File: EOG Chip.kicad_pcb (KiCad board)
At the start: 2 copper layers, 15 parts, among them U1 INA128, U2 INA128, U3 TL074

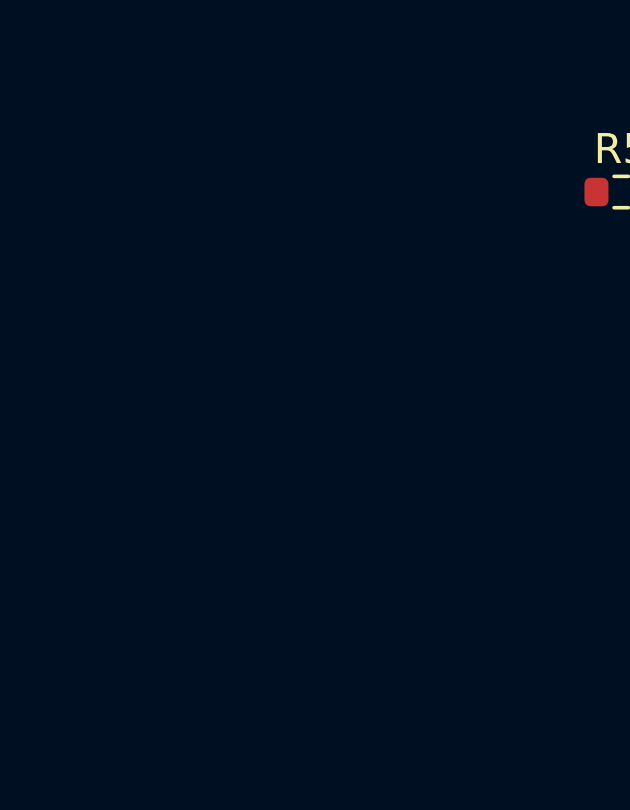
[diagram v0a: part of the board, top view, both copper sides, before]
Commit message: Added footprints for antenna filter module and microcontroller
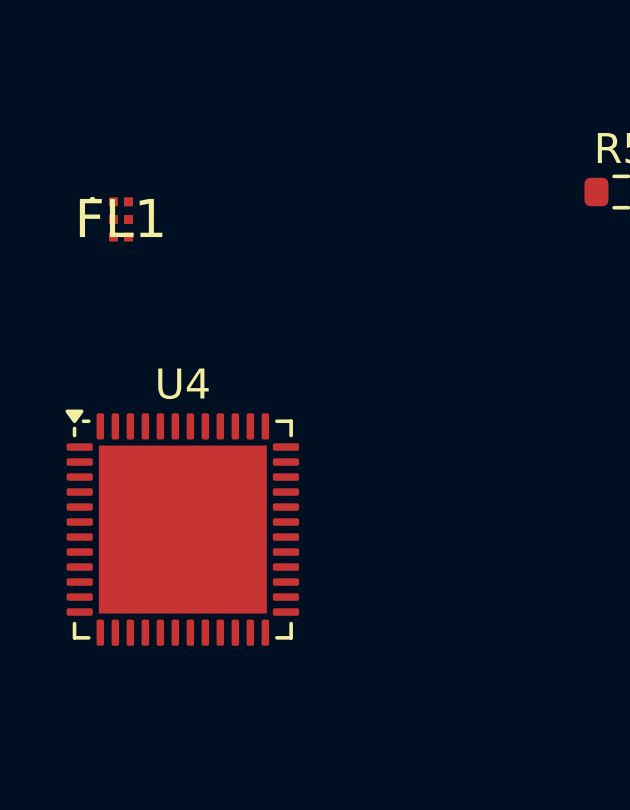
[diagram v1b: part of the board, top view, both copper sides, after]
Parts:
- added FL1: MLPF-WB55-01E3, AntennaFilter_MLPF:BUMPLESS_CSP_2025, F.Cu at (126.5, 86.4)
- added U4: STM32WB55CCUx, Package_DFN_QFN:QFN-48-1EP_7x7mm_P0.5mm_EP5.6x5.6mm, F.Cu at (128.6, 96.8)
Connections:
- R5 pad 2: GND -> GROUND
- R6 pad 1: +5V -> +3V

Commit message: updated files
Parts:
- added AE1: Antenna, antenna_ghz:ANTC3216X60N, F.Cu at (132.5, 107.5)
- added Y1: Crystal, new_crystal:ABM11A32000MHZD2YT3, F.Cu at (179.3, 105.0)
- FL1: footprint AntennaFilter_MLPF:BUMPLESS_CSP_2025 -> a_rf_module:BUMPLESS_CSP_2025
- moved R_GAIN_HOR1 49.2 mm to (114.1, 77.5), turned to 90 degrees
- moved R1 45.2 mm to (152.8, 55.0)
- moved R_GAIN_VERT1 44.0 mm to (114.7, 95.4), turned to 90 degrees
- moved R3 41.4 mm to (129.8, 72.5)
- moved U2 38.3 mm to (121.4, 103.0), turned to 90 degrees
- moved U1 38.1 mm to (121.5, 82.5), turned to 90 degrees
- moved U4 37.6 mm to (165.7, 102.9)
- moved C1 35.9 mm to (139.1, 72.5), turned to 0 degrees
- moved R2 24.8 mm to (170.0, 90.0)
- moved R4 24.7 mm to (128.9, 90.4)
- moved FL1 23.3 mm to (139.8, 105.6)
- moved R5 22.9 mm to (160.0, 70.0)
- moved R6 22.9 mm to (164.5, 70.0)
- moved U3 12.4 mm to (151.2, 77.4)
- moved C2 11.0 mm to (138.9, 90.4), turned to 0 degrees
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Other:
- board outline added: 80 x 50 mm

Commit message: updating schematics
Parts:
- U1, U2: footprint Package_DIP:DIP-8_W7.62mm -> amp_new:SOP65P490X110-8N
- U3: footprint Package_DIP:DIP-14_W7.62mm -> amp_new_big:SOIC127P600X175-14N
- moved C3 34.5 mm to (163.2, 71.0)
- moved R5 24.4 mm to (169.5, 92.5)
- moved R6 24.0 mm to (165.0, 94.0)
- moved R2 23.5 mm to (147.0, 95.0)
- moved R1 16.2 mm to (150.2, 71.0)
- moved FL1 12.5 mm to (152.2, 106.5)
- moved AE1 10.5 mm to (143.0, 107.0)
- moved C4 7.26 mm to (147.0, 101.0)
- moved Y1 6.82 mm to (172.5, 105.0)
- moved C2 4.88 mm to (138.9, 85.5)
- moved R3 4.14 mm to (125.9, 71.0)
- moved R4 2.09 mm to (126.8, 90.4)
- moved C1 1.50 mm to (139.1, 71.0)
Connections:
- U3 pad 13: Net-(U2-Ref) -> Net-(U1-Ref)
- U3 pad 14: Net-(U2-Ref) -> Net-(U1-Ref)
- U3 pad 8: Net-(U1-Ref) -> Net-(U2-Ref)
- U3 pad 9: Net-(U1-Ref) -> Net-(U2-Ref)
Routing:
- added copper zone on B.Cu, net GND
- added copper zone on F.Cu, net GND

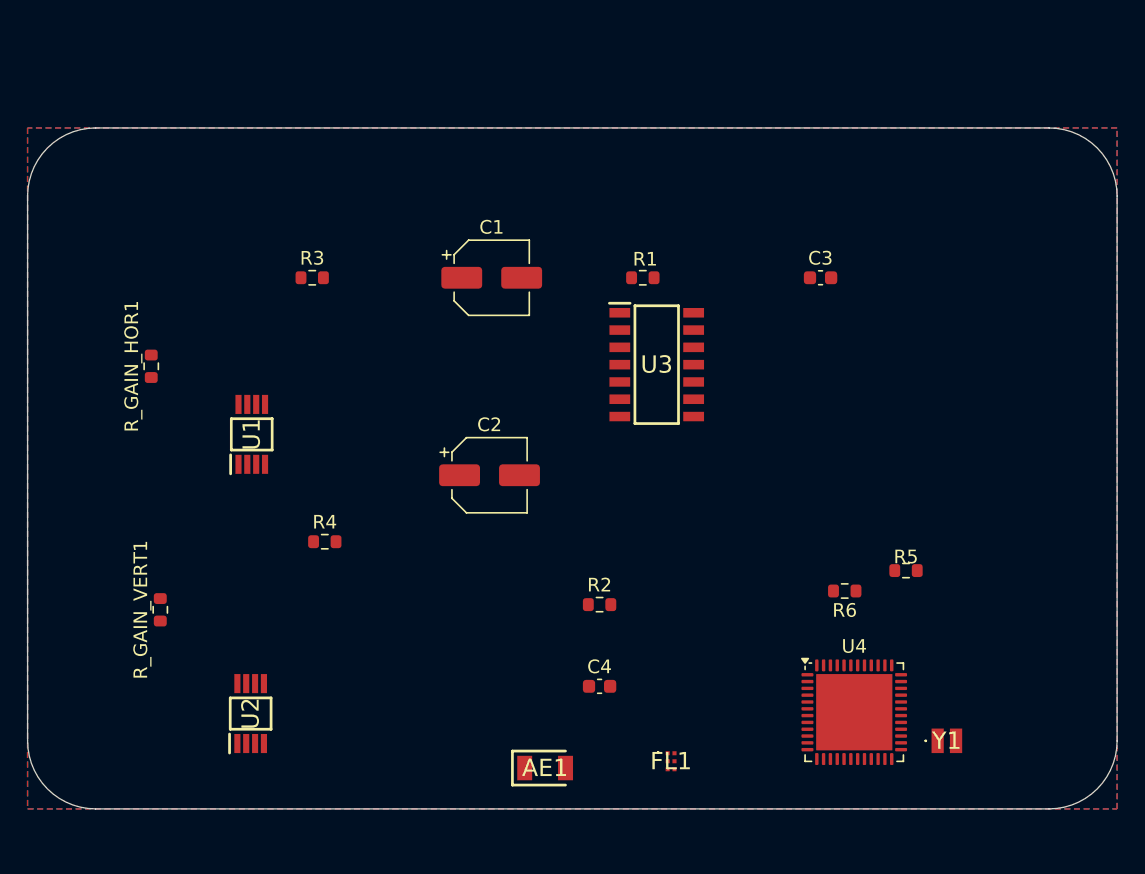
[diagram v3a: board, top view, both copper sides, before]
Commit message: Added potentiometers and started on traces
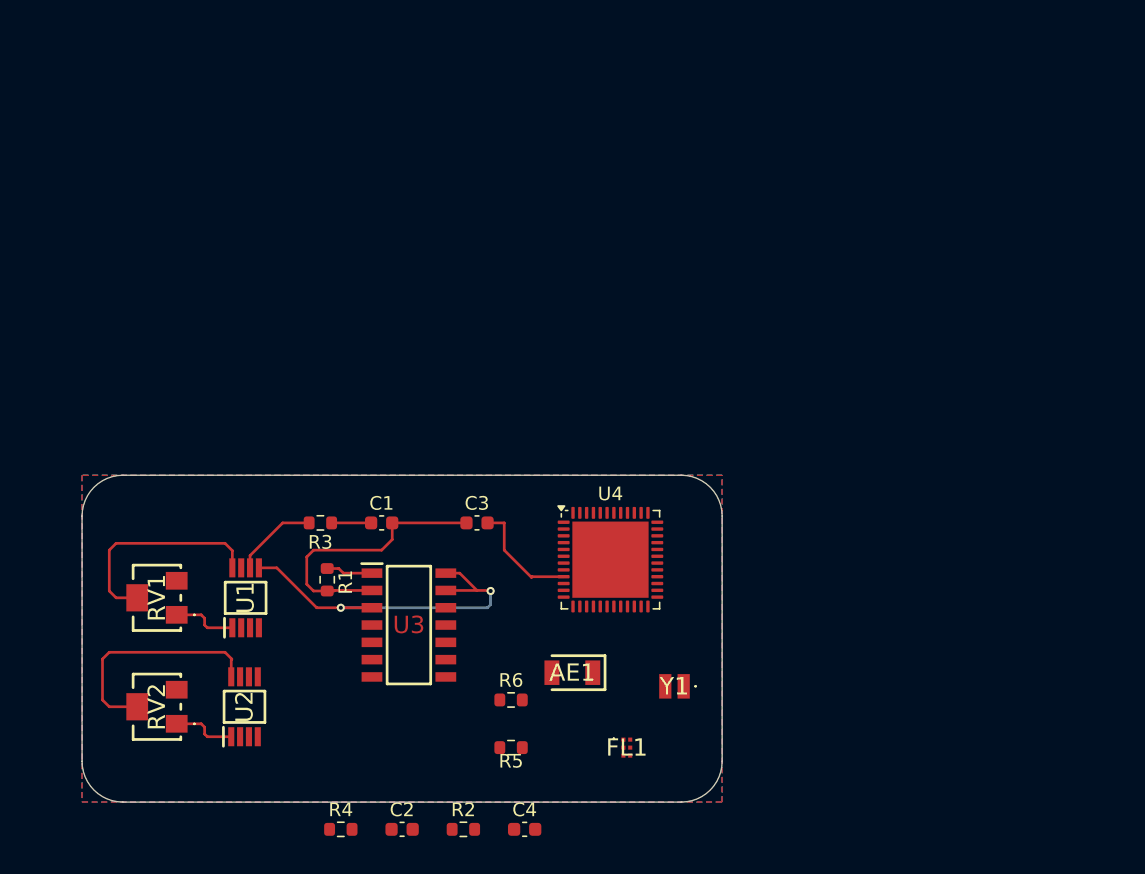
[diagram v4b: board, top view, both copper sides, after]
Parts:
- C1, C2: value C_Polarized_US -> C; footprint Capacitor_SMD:CP_Elec_5x4.5 -> Capacitor_SMD:C_0603_1608Metric
- RV1: renamed from R_GAIN_HOR1; value R -> R_Potentiometer_Hor; footprint Resistor_SMD:R_0603_1608Metric -> Potentiometer_TSM:TSM41YJ503KR05
- RV2: renamed from R_GAIN_VERT1; value R -> R_Potentiometer_Vert; footprint Resistor_SMD:R_0603_1608Metric -> Potentiometer_TSM:TSM41YJ503KR05
- moved R1 32.1 mm to (127.0, 93.2), turned to -90 degrees
- moved R5 31.8 mm to (140.5, 105.5), turned to 180 degrees
- moved C3 31.0 mm to (138.0, 89.0)
- moved C2 26.8 mm to (132.5, 111.5)
- moved U3 26.4 mm to (133.0, 96.5)
- moved R6 25.8 mm to (140.5, 102.0), turned to 0 degrees
- moved R4 21.2 mm to (128.0, 111.5)
- moved U4 21.1 mm to (147.8, 91.7)
- moved Y1 20.4 mm to (152.5, 101.0), turned to 180 degrees
- moved C1 19.7 mm to (131.0, 89.0)
- moved R2 19.3 mm to (137.0, 111.5)
- moved R3 18.0 mm to (126.5, 89.0), turned to 180 degrees
- moved RV1 17.0 mm to (114.5, 94.5)
- moved U1 12.0 mm to (121.0, 94.5)
- moved C4 11.9 mm to (141.5, 111.5)
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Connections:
- U4 pad 10: HOR_OUT -> VERT_OUT
- U4 pad 9: VERT_OUT -> HOR_OUT
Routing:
- net Net-(U1-Ref): track 0.00 -> 27.7 mm, vias 0 -> 2
- net Net-(U3A--): track 0.00 -> 20.5 mm
- net Net-(RV2-Pad2): track 0.00 -> 17.0 mm
- net Net-(RV1-Pad2): track 0.00 -> 16.0 mm
- net HOR_OUT: track 0.00 -> 8.44 mm
- net Net-(R3-Pad2): track 0.00 -> 6.23 mm
- net Net-(RV1-Pad1): track 0.00 -> 4.77 mm
- net Net-(RV2-Pad1): track 0.00 -> 4.69 mm
- net Net-(R1-Pad1): track 0.00 -> 3.45 mm
- net Net-(C1-Pad1): track 0.00 -> 2.90 mm
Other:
- board size 80 x 50 mm -> 47 x 24 mm

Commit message: Add files via upload
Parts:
- moved R2 14.1 mm to (126.8, 101.8), turned to -90 degrees
- moved C4 8.68 mm to (135.3, 105.4)
- moved R4 6.98 mm to (125.0, 105.2), turned to 180 degrees
- moved C2 6.84 mm to (129.6, 105.3)
- moved AE1 1.65 mm to (145.4, 101.6)
- moved Y1 0.29 mm to (152.8, 100.9)
- turned R5 to 0 degrees
- turned R6 to 180 degrees
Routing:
- net Net-(U2-Ref): track 0.00 -> 23.9 mm, vias 0 -> 3
- net Net-(FL1-IN): track 0.00 -> 17.7 mm
- net VERT_OUT: track 0.00 -> 16.5 mm
- net REF_IN: track 0.00 -> 15.8 mm, vias 0 -> 2
- net +3V: track 0.00 -> 13.0 mm
- net Net-(R4-Pad2): track 0.00 -> 10.8 mm
- net Net-(U3B--): track 0.00 -> 10.2 mm
- net Net-(U4-OSC_IN): track 0.00 -> 8.25 mm
- net Net-(U4-OSC_OUT): track 0.00 -> 6.40 mm
- net Net-(AE1-A): track 0.00 -> 4.90 mm
- net Net-(R2-Pad1): track 0.00 -> 3.76 mm
- net Net-(C2-Pad1): track 0.00 -> 3.04 mm

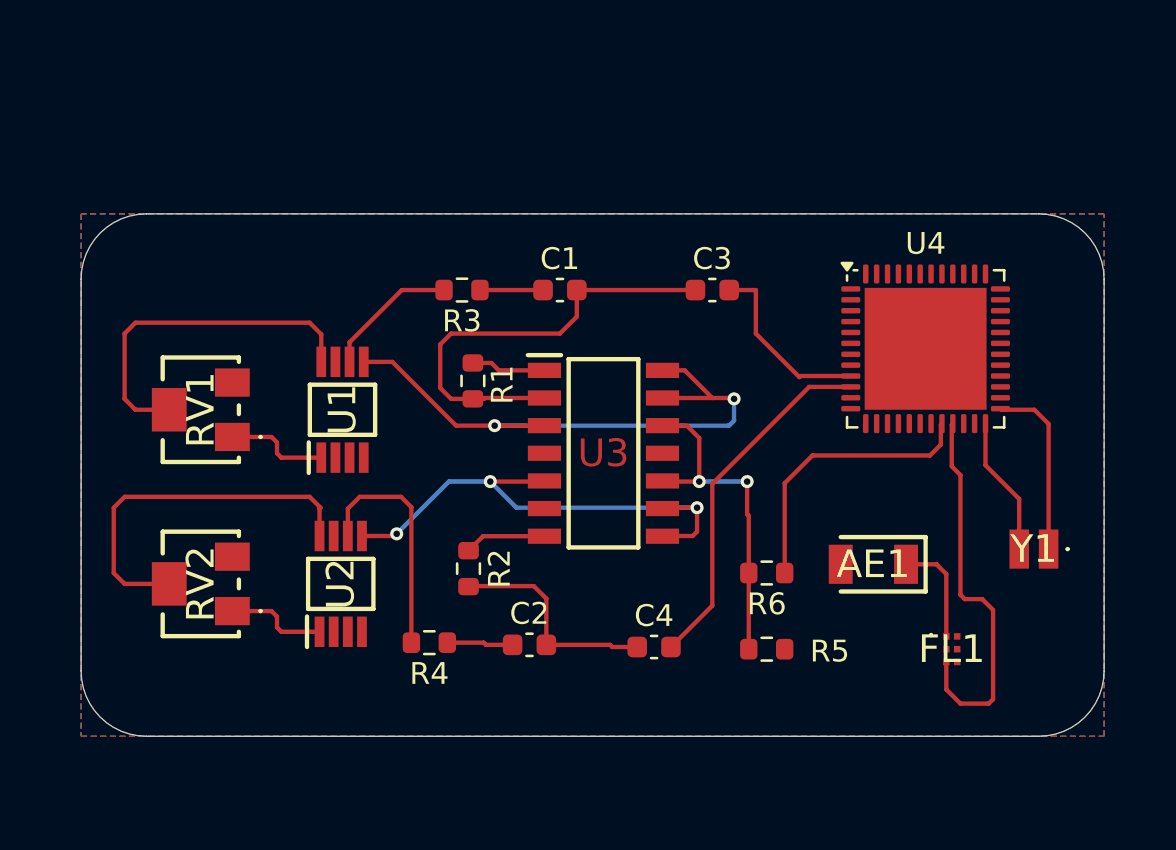
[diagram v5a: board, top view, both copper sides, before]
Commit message: updated schematic and pcb
traces are almost finished
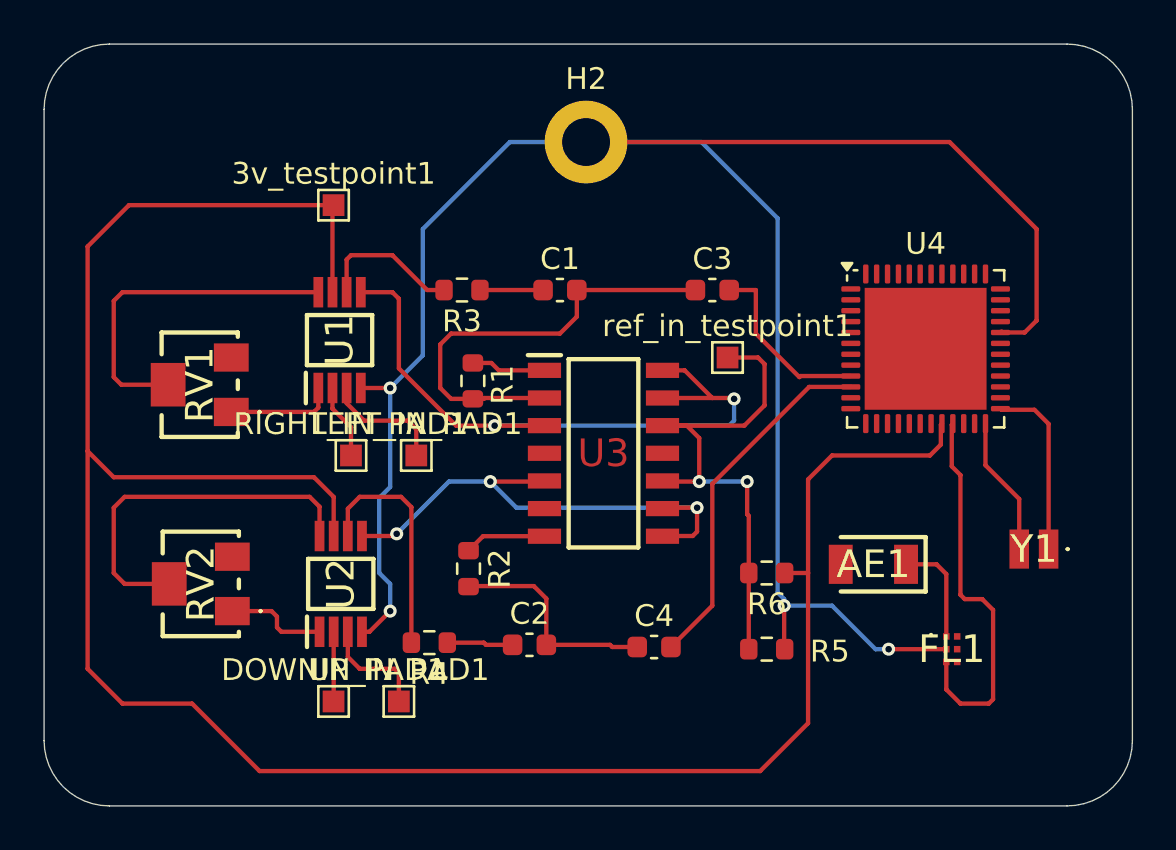
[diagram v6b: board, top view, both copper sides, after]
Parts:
- added 3v_testpoint1: TestPoint, TestPoint:TestPoint_Pad_1.0x1.0mm, F.Cu at (120.6, 85.1)
- added DOWNIN_PAD1: TestPoint, TestPoint:TestPoint_Pad_1.0x1.0mm, F.Cu at (120.6, 107.9)
- added H2: Ground_Pad, MountingHole:MountingHole_2.2mm_M2_DIN965_Pad, F.Cu at (132.2, 82.2)
- added LEFT_IN_PAD1: TestPoint, TestPoint:TestPoint_Pad_1.0x1.0mm, F.Cu at (124.4, 96.6)
- added RIGHT_IN_PAD1: TestPoint, TestPoint:TestPoint_Pad_1.0x1.0mm, F.Cu at (121.4, 96.6)
- added UP_IN_PAD1: TestPoint, TestPoint:TestPoint_Pad_1.0x1.0mm, F.Cu at (123.6, 107.9)
- added ref_in_testpoint1: TestPoint, TestPoint:TestPoint_Pad_1.0x1.0mm, F.Cu at (138.7, 92.1)
- moved U1 3.20 mm to (120.9, 91.3)
- moved RV1 1.15 mm to (114.5, 93.3)
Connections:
- FL1 pad A2: GROUND -> GND
- R5 pad 2: GROUND -> GND
- U1 pad 7: +5V -> +3V
- U2 pad 7: +5V -> +3V
- U4 pad 22: GROUND -> GND
- U4 pad 32: GROUND -> GND
- U4 pad 49: GROUND -> GND
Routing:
- net GND: track 0.00 -> 97.8 mm, vias 0 -> 4
- net +3V: track 13.0 -> 105.5 mm
- net REF_IN: track 15.8 -> 24.6 mm
- net LEFT_IN: track 0.00 -> 5.60 mm
- net UP_IN: track 0.00 -> 5.11 mm
- net RIGHT_IN: track 0.00 -> 3.45 mm
- net Net-(U1-Ref): track 27.7 -> 31.1 mm
- net DOWN_IN: track 0.00 -> 3.20 mm
- removed copper zone on B.Cu, net GND
- removed copper zone on F.Cu, net GND
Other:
- board size 47 x 24 mm -> 50 x 35 mm

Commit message: updated pcb and schematic
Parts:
- added H1: MountingHole, MountingHole:MountingHole_2mm, F.Cu at (110.3, 80.7)
- added H3: MountingHole, MountingHole:MountingHole_2mm, F.Cu at (154.3, 80.7)
- added H4: MountingHole, MountingHole:MountingHole_2mm, F.Cu at (154.3, 109.7)
- added H5: MountingHole, MountingHole:MountingHole_2mm, F.Cu at (110.3, 109.7)
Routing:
- added copper zone on B.Cu, net GND
- added copper zone on F.Cu, net GND
